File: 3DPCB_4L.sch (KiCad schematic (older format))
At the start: 194 parts, among them IC1 DRV8825, IC2 DRV8825, IC3 DRV8825, IC4 DRV8825, IC5 DRV8825, J1 SOLDER_JUMPER_3P, J10 , J11 , J12 , J13 , J14 , J15 , J16 , J2 , J3 , J4 , J5 , J6 , J7 , J8 , J9 , K1 CONN_3, K2 CONN_3, K3 CONN_3, K4 CONN_3, K5 CONN_3, K6 CONN_3, K7 CONN_3, K8 CONN_3, K9 CONN_3, P1 CONN_8, P10 CONN_2, P11 CONN_3X2, P12 CONN_3X2, P13 CONN_4, P2 CONN_2, P3 CONN_2, P4 CONN_2, P5 CONN_4, P6 CONN_4, P7 CONN_4, P8 CONN_2, P9 CONN_4, U1 CONN_4_LERCHE, U10 MICRO-SD, U11 TC4427, U12 MCP4728, U13 CONN_4_LERCHE, U15 SPST_MOMENTARY, U16 CONN_4_LERCHE, U17 TC4427, U2 SPST_MOMENTARY, U20 TPS6213X, U21 CONN_4_LERCHE, U22 CONN_4_LERCHE, U23 MCP4728, U24 MOS_NFET, U25 CONN_4_LERCHE, U3 BSS84, U4 CONN_4_LERCHE, U5 MOS_NFET, U6 LPC1768_TQFP100, U7 MOS_NFET, U8 MOS_NFET

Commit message: Trying MP9943 DC to DC
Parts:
- removed C47: 3.3nF, ~, symbol C
- removed U20: TPS6213X, symbol TPS6213X
- added C?: 100uF, ~, symbol CP
- added C?: 100n, ~, symbol C
- added IC?: MP9943, ~, symbol MP9943
- added R?: 1M, ~, symbol R
- added R?: 20R, ~, symbol R
- added R?: 51k, ~, symbol R
- added R?: 41k2, ~, symbol R
- added R?: 13k, ~, symbol R
- C43: value 100uF -> 47uF
- L2: value INDUCTOR -> 10uH
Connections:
- wire segments 394 -> 401
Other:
- moved on the sheet: C2, C44, C45, C46, C6, D9, L2

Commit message: Needs to make MP9943 footprint for PCB
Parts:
- gave numbers to parts that had none: 9

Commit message: PCB routed, needs specific BOM
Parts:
- removed C48, C49, C56, C57, C58, C59, C60, C61: 100n, ~, symbol C
- removed C55: 10uF, ~, symbol CP
- removed D10: DIODE, ~, symbol DIODE
- removed J1: SOLDER_JUMPER_3P, ~, symbol SOLDER_JUMPER_3P
- removed P10, P2, P3, P4: CONN_2, symbol CONN_2
- removed R17, R25, R26, R49, R50, R51: 1k, ~, symbol R
- removed R46, R47, R48, R52, R53, R54: 5k6, ~, symbol R
- removed VREG1: AMS1117, ~, symbol AMS1117
- added P2: CONN_8, symbol CONN_8
- added R56, R57, R58, R59: 3k, ~, symbol R
- L2: value 10uH -> IHLP1212-10uH
- R14, R15, R16, R20: value 4K7 -> 9k
- U11, U17: value TC4427 -> IX4427
- U24, U5, U7, U8: value MOS_NFET -> IRFH7932
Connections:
- net labels added: P2.4, P2.5, VDCVDC
- net labels removed: +5V, PWM0, PWM1, X-MAX-LPC, X-MIN-LPC, Y-MAX-LPC, Y-MIN-LPC, Z-MAX-LPC, Z-MIN-LPC
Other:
- note removed: "MOSFET: IRFH7932"
- note removed: "MOSFETS: STL60N3LLH5"
- moved on the sheet: K1, K2, K3, K4, K5, K6, R14, R15, R16, R20, U11A, U11B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

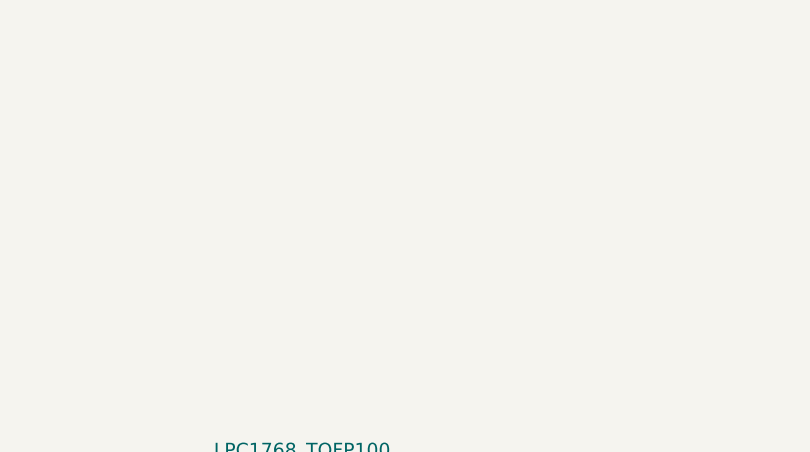
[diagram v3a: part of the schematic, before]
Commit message: All PCB is routed - PCB sent to production
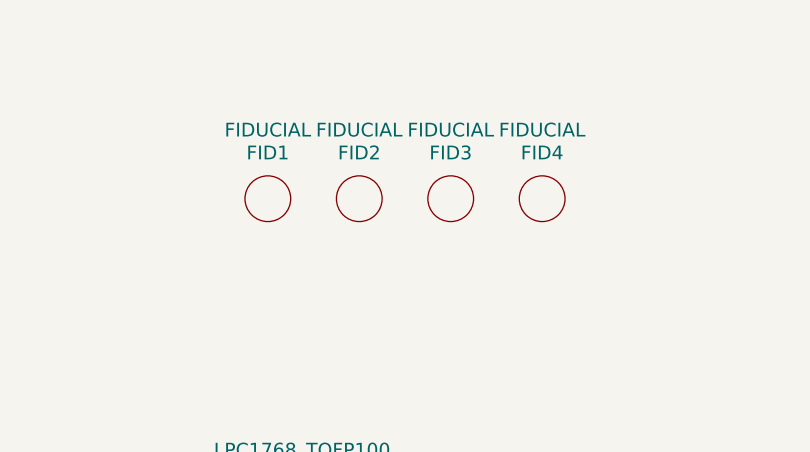
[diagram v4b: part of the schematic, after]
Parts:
- added FID1, FID2, FID3, FID4: FIDUCIAL, symbol FIDUCIAL
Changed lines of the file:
@@
 Sheet 1 1
 Title "3DPCB"
-Date "24 aug 2015"
+Date "14 sep 2015"
 Rev "C"
 Comp "LercheTech"
@@
 Connection ~ 13400 13150
 Connection ~ 13400 12950
+$Comp
+L FIDUCIAL FID1
+U 1 1 55F69685
+P 7100 1050
+F 0 "FID1" H 7100 1250 60  0000 C CNN
+F 1 "FIDUCIAL" H 7100 1350 60  0000 C CNN
+F 2 "" H 7100 1050 60  0000 C CNN
+F 3 "" H 7100 1050 60  0000 C CNN
+	1    7100 1050
+	1    0    0    -1
+$EndComp
+$Comp
+L FIDUCIAL FID2
+U 1 1 55F69692
+P 7500 1050
+F 0 "FID2" H 7500 1250 60  0000 C CNN
+F 1 "FIDUCIAL" H 7500 1350 60  0000 C CNN
+F 2 "" H 7500 1050 60  0000 C CNN
+F 3 "" H 7500 1050 60  0000 C CNN
+	1    7500 1050
+	1    0    0    -1
+$EndComp
+$Comp
+L FIDUCIAL FID3
+U 1 1 55F69698
+P 7900 1050
+F 0 "FID3" H 7900 1250 60  0000 C CNN
+F 1 "FIDUCIAL" H 7900 1350 60  0000 C CNN
+F 2 "" H 7900 1050 60  0000 C CNN
+F 3 "" H 7900 1050 60  0000 C CNN
+	1    7900 1050
+	1    0    0    -1
+$EndComp
+$Comp
+L FIDUCIAL FID4
+U 1 1 55F6969E
+P 8300 1050
+F 0 "FID4" H 8300 1250 60  0000 C CNN
+F 1 "FIDUCIAL" H 8300 1350 60  0000 C CNN
+F 2 "" H 8300 1050 60  0000 C CNN
+F 3 "" H 8300 1050 60  0000 C CNN
+	1    8300 1050
+	1    0    0    -1
+$EndComp
 $EndSCHEMATC

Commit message: Removed soldermask from stackup-info
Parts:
- U24, U5, U7, U8: value IRFH7932 -> IRFH5302
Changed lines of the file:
@@
 Sheet 1 1
 Title "3DPCB"
-Date "14 sep 2015"
+Date "15 sep 2015"
 Rev "C"
 Comp "LercheTech"
@@
 P 9250 13250
 F 0 "U5" H 9650 13200 60  0000 C CNN
-F 1 "IRFH7932" H 9650 13300 60  0000 C CNN
+F 1 "IRFH5302" H 9650 13300 60  0000 C CNN
 F 2 "~" H 9350 13250 60  0000 C CNN
 F 3 "~" H 9350 13250 60  0000 C CNN
@@
 P 11900 13250
 F 0 "U7" H 12300 13200 60  0000 C CNN
-F 1 "IRFH7932" H 12300 13300 60  0000 C CNN
+F 1 "IRFH5302" H 12300 13300 60  0000 C CNN
 F 2 "~" H 12000 13250 60  0000 C CNN
 F 3 "~" H 12000 13250 60  0000 C CNN
@@
 P 9250 14500
 F 0 "U8" H 9650 14450 60  0000 C CNN
-F 1 "IRFH7932" H 9650 14550 60  0000 C CNN
+F 1 "IRFH5302" H 9650 14550 60  0000 C CNN
 F 2 "~" H 9350 14500 60  0000 C CNN
 F 3 "~" H 9350 14500 60  0000 C CNN
@@
 P 11900 14500
 F 0 "U24" H 12300 14450 60  0000 C CNN
-F 1 "IRFH7932" H 12300 14550 60  0000 C CNN
+F 1 "IRFH5302" H 12300 14550 60  0000 C CNN
 F 2 "~" H 12000 14500 60  0000 C CNN
 F 3 "~" H 12000 14500 60  0000 C CNN

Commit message: Added LercheTech library
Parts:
- C1, C12, C13, C14, C15, C16, C17, C18, C19, C2, C20, C22, C23, C28, C29, C30, C31, C32, C33, C34, C35, C36, C37, C38, C39, C40, C41, C42, C44, C45, C46, C5, C50, C51, C52, C53, C54, C6, C64, C65, C67, C68, C69, C71, C8, C9: symbol C -> C-RESCUE-3DPCB_4L
- C10, C11, C24, C25, C26, C27, C3, C4, C43, C7, C70: symbol CP -> CP-RESCUE-3DPCB_4L
- D1, D2, D3, D4, D6, D7, D8: symbol LED -> LED-RESCUE-3DPCB_4L
- R1, R10, R11, R12, R13, R14, R15, R16, R18, R19, R2, R20, R21, R22, R23, R24, R27, R28, R29, R3, R30, R31, R32, R33, R34, R35, R36, R37, R38, R39, R4, R40, R41, R42, R43, R44, R45, R5, R55, R56, R57, R58, R59, R6, R7, R8, R9: symbol R -> R-RESCUE-3DPCB_4L

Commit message: Updated
local repository + minor change to allow 24V on MOSFET drivers.
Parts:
- removed U17: IX4427, symbol TC4427
- added C21, C47: 100n, LercheTech:Lerche_C0603, symbol C-RESCUE-3DPCB_4L
- added C49: 1uF, LercheTech:Lerche_C0603, symbol C
- added D10: Vz10V/0.5W, Diodes_SMD:SMA_Standard, symbol ZENERsmall
- added R17: 1k, Resistors_SMD:R_0805, symbol R
- added U9: TC4427, SMD_Packages:SOIC-8-N, symbol TC4427
- C1, C12, C13, C14, C15, C16, C17, C18, C19, C2, C20, C22, C23, C28, C29, C30, C31, C32, C33, C34, C35, C36, C37, C38, C39, C40, C41, C42, C44, C45, C46, C5, C50, C51, C52, C53, C54, C6, C64, C65, C67, C68, C69, C71, C8, C9: footprint ~ -> LercheTech:Lerche_C0603
- C10, C3, C4, C7: footprint ~ -> Capacitors_Tantalum_SMD:TantalC_SizeA_EIA-3216_Reflow
- C11, C24, C25, C26, C27, C70: footprint ~ -> Capacitors_ThroughHole:C_Radial_D6.3_L11.2_P2.5
- C43: footprint ~ -> Capacitors_SMD:c_elec_5x5.8
- CONN1: footprint ~ -> LercheTech:Lerche_MINI_USB
- D1, D2, D3, D4, D6, D7, D8: footprint ~ -> LEDs:LED_0603
- D5, D9: footprint ~ -> LercheTech:Lerche_SOD323
- FID1, FID2, FID3, FID4: footprint (none) -> LercheTech:Lerche_Fiducial
- IC1, IC2, IC3, IC4, IC5: footprint ~ -> LercheTech:Lerche_TSSOP28_EP
- IC6: footprint ~ -> LercheTech:Lerche_MP9943
- J10, J11, J12, J13, J14, J15, J16, J2, J3, J4, J5, J6, J7, J8, J9: footprint ~ -> LercheTech:Lerche_2PsolderJumper
- K1, K2, K3, K4, K5, K6, K8, K9: footprint (none) -> Pin_Headers:Pin_Header_Straight_1x03
- K7: footprint (none) -> LercheTech:Lerche_3P_1.27MM
- L1, R1, R10, R11, R12, R13, R18, R19, R2, R27, R28, R3, R34, R35, R36, R38, R39, R4, R40, R41, R42, R43, R44, R45, R5, R55, R6, R7, R8, R9: footprint ~ -> LercheTech:Lerche_R0603
- L2: footprint ~ -> LercheTech:Lerche_IHLP-1212BZ-11_Inductor
- OSC1: footprint (none) -> LercheTech:Lerche_Oscillator_2.5x2.0mm
- P1: footprint (none) -> LercheTech:Lerche_8P_2.54mm
- P11: footprint (none) -> Pin_Headers:Pin_Header_Straight_2x03
- P12: footprint (none) -> LercheTech:Lerche_6P_1.6mm_2ROW
- P13, P5, P6, P7, P9: footprint (none) -> LercheTech:Lerche_4P_2.54mm
- P2: footprint (none) -> LercheTech:Lerche_8P_CONN_3,5mm
- P8: footprint (none) -> LercheTech:Lerche_2P_5MM
- R14, R15, R16, R20: value 9k -> 47k; footprint ~ -> LercheTech:Lerche_R0603
- R21, R22, R23, R24, R29, R30, R31, R32, R33, R37: footprint ~ -> LercheTech:Lerche_R1206
- R56, R57, R58, R59: value 3k -> 10R; footprint ~ -> LercheTech:Lerche_R0603
- U1, U13, U16, U21, U22, U25, U4: footprint ~ -> LercheTech:Lerche_4P_2.54mm
- U10: footprint (none) -> LercheTech:Lerche_Molex_502774-0891
- U11: value IX4427 -> TC4427; footprint (none) -> SMD_Packages:SOIC-8-N
- U12, U23: footprint (none) -> LercheTech:Lerche_MSOP-10
- U15, U2: footprint ~ -> LercheTech:Lerche_SPST_ITEAD
- U24, U5, U7, U8: footprint ~ -> LercheTech:Lerche_PQFN_5x6B
- U3: footprint ~ -> LercheTech:Lerche_SOT23-3
- U6: footprint ~ -> Housings_QFP:TQFP-100_14x14mm_Pitch0.5mm
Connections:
- net +12V: now also R17.1; no longer U11.6 (Vdd), U11.6 (Vdd)
- net GND: now also C21.2, C47.2, C49.2, D10.2 (A), U9.3 (GND); no longer U11.3 (GND)
- net P2.4: now also U9.2 (IN)
- net P2.5: now also U9.4 (IN)
- net at R56.1: now also U9.7 (OUT)
- net at R58.1: now also U9.5 (OUT)
- new net MOSVCC: C21.1, C47.1, C49.1, D10.1 (K), R17.2, U11.6 (Vdd), U9.6 (Vdd)
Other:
- note added: "+24V connector"
- note added: "Caps for stepper drivers"
- note added: "DAC's for stepper current control"
- note added: "DC/DC Converter"
- note added: "Endstop inputs"
- note added: "I2C connection"
- note added: "LED's"
- note added: "MOSFET outputs"
- note added: "Micro-SD"
- note added: "Pinheader output for stepper drivers"
- note added: "Provided as-is.\nThis is 3DPCB, a board for driving 3D printers, CNC's and what else is possible using the onboard equipment. \nThe design is based around Smoothieware, and Smoothieboard, but some things are done differently. \nThe onboard DC/DC converter makes it possible to connect up to maximum 27V, and drive the steppers with this voltage. \n"
- note added: "Reset and Play button"
- note added: "SPI pinout"
- note added: "SPI_SD pinout"
- note added: "Stepper drivers"
- note added: "Thermistor inputs"
- note added: "Todo: Switch to IRFH7085TRPBF MOSFET transistors"
- note added: "UART0 pinout"
- note added: "USB connector"
- moved on the sheet: C22, C23, C24, C25, C26, C27, C28, C29, C30, C31, C32, C33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

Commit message: Updated PCB
Updated PCB, splitting power for MOSFETs and motor-drivers.
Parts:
- removed P8: CONN_2, LercheTech:Lerche_2P_5MM, symbol CONN_2
- added P8: CONN_02X03, symbol CONN_02X03
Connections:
- net +12V: now also P8.2 (P2); no longer P2.2 (P2), P2.4 (P4), P2.6 (P6), P2.8 (P8), R17.1
- net GND: now also P8.1 (P1), P8.4 (P4), P8.6 (P6)
- new net V_MOSFET: P2.2 (P2), P2.4 (P4), P2.6 (P6), P2.8 (P8), P8.3 (P3), P8.5 (P5), R17.1
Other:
- note added: "Molex UltraFit power connector"
- note added: "Todo: Switch to IRFH7085TRPBF MOSFETs"
- note removed: "+24V connector"
- note removed: "Todo: Switch to IRFH7085TRPBF MOSFET transistors"
- moved on the sheet: K7, P11
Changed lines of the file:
@@
 LIBS:contrib
 LIBS:valves
-LIBS:lerchetech (1)
+LIBS:lerchetech
 LIBS:3DPCB_4L-cache
 EELAYER 25 0
@@
 P2.6
 $Comp
-L +12V #PWR87
-U 1 1 524C0A34
-P 15450 10600
-F 0 "#PWR87" H 15450 10550 20  0001 C CNN
-F 1 "+12V" H 15450 10700 30  0000 C CNN
-F 2 "" H 15450 10600 60  0000 C CNN
-F 3 "" H 15450 10600 60  0000 C CNN
-	1    15450 10600
-	1    0    0    -1
-$EndComp
-$Comp
 L C-RESCUE-3DPCB_4L C16
 U 1 1 524C17C4
@@
 L GND-RESCUE-3DPCB_4L #PWR7
 U 1 1 524B7E4F
-P 1350 4400
-F 0 "#PWR7" H 1350 4400 30  0001 C CNN
-F 1 "GND" H 1350 4330 30  0001 C CNN
-F 2 "" H 1350 4400 60  0000 C CNN
-F 3 "" H 1350 4400 60  0000 C CNN
-	1    1350 4400
+P 1750 4500
+F 0 "#PWR7" H 1750 4500 30  0001 C CNN
+F 1 "GND" H 1750 4430 30  0001 C CNN
+F 2 "" H 1750 4500 60  0000 C CNN
+F 3 "" H 1750 4500 60  0000 C CNN
+	1    1750 4500
 	1    0    0    -1
 $EndComp
@@
 L +12V #PWR6
 U 1 1 524B816D
-P 1350 3950
-F 0 "#PWR6" H 1350 3900 20  0001 C CNN
-F 1 "+12V" H 1350 4050 30  0000 C CNN
-F 2 "" H 1350 3950 60  0000 C CNN
-F 3 "" H 1350 3950 60  0000 C CNN
-	1    1350 3950
+P 1750 4100
+F 0 "#PWR6" H 1750 4050 20  0001 C CNN
+F 1 "+12V" H 1750 4200 30  0000 C CNN
+F 2 "" H 1750 4100 60  0000 C CNN
+F 3 "" H 1750 4100 60  0000 C CNN
+	1    1750 4100
 	1    0    0    -1
 $EndComp
@@
 L CONN_3 K7
 U 1 1 5253846A
-P 1650 4150
-F 0 "K7" V 1600 4150 50  0000 C CNN
-F 1 "CONN_3" V 1700 4150 40  0000 C CNN
-F 2 "LercheTech:Lerche_3P_1.27MM" H 1650 4150 60  0001 C CNN
-F 3 "" H 1650 4150 60  0000 C CNN
-	1    1650 4150
+P 2350 4150
+F 0 "K7" V 2300 4150 50  0000 C CNN
+F 1 "CONN_3" V 2400 4150 40  0000 C CNN
+F 2 "LercheTech:Lerche_3P_1.27MM" H 2350 4150 60  0001 C CNN
+F 3 "" H 2350 4150 60  0000 C CNN
+	1    2350 4150
 	-1   0    0    -1
 $EndComp
-Text GLabel 2000 4050 2    39   Input ~ 0
+Text GLabel 2700 4050 2    39   Input ~ 0
 TX_0
-Text GLabel 2000 4150 2    39   Input ~ 0
+Text GLabel 2700 4150 2    39   Input ~ 0
 RX_0
-Text GLabel 2000 4250 2    39   Input ~ 0
+Text GLabel 2700 4250 2    39   Input ~ 0
 GND
 Text Label 11550 10850 2    39   ~ 0
@@
 PLAY_LED
 $Comp
-L CONN_2 P8
-U 1 1 5258344A
-P 1000 4150
-F 0 "P8" V 950 4150 40  0000 C CNN
-F 1 "CONN_2" V 1050 4150 40  0000 C CNN
-F 2 "LercheTech:Lerche_2P_5MM" H 1000 4150 60  0001 C CNN
-F 3 "" H 1000 4150 60  0000 C CNN
-	1    1000 4150
-	-1   0    0    1
-$EndComp
-$Comp
 L +3.3V-RESCUE-3DPCB_4L #PWR3
 U 1 1 52584578
@@
 L GND-RESCUE-3DPCB_4L #PWR33
 U 1 1 525FF499
-P 2500 4350
-F 0 "#PWR33" H 2500 4350 30  0001 C CNN
-F 1 "GND" H 2500 4280 30  0001 C CNN
-F 2 "" H 2500 4350 60  0000 C CNN
-F 3 "" H 2500 4350 60  0000 C CNN
-	1    2500 4350
+P 3200 4350
+F 0 "#PWR33" H 3200 4350 30  0001 C CNN
+F 1 "GND" H 3200 4280 30  0001 C CNN
+F 2 "" H 3200 4350 60  0000 C CNN
+F 3 "" H 3200 4350 60  0000 C CNN
+	1    3200 4350
 	-1   0    0    -1
 $EndComp
-Text GLabel 3400 4050 2    39   Input ~ 0
+Text GLabel 4100 4050 2    39   Input ~ 0
 SSEL1
-Text GLabel 2600 4050 0    39   Input ~ 0
+Text GLabel 3300 4050 0    39   Input ~ 0
 MISO1
-Text GLabel 2600 4150 0    39   Input ~ 0
+Text GLabel 3300 4150 0    39   Input ~ 0
 MOSI1
-Text GLabel 3400 4150 2    39   Input ~ 0
+Text GLabel 4100 4150 2    39   Input ~ 0
 SCK1
 $Comp
@@
 L CONN_3X2 P11
 U 1 1 5368F485
-P 3000 4200
-F 0 "P11" H 3000 4450 50  0000 C CNN
-F 1 "CONN_3X2" V 3000 4250 40  0000 C CNN
-F 2 "Pin_Headers:Pin_Header_Straight_2x03" H 3000 4200 60  0001 C CNN
-F 3 "" H 3000 4200 60  0000 C CNN
-	1    3000 4200
+P 3700 4200
+F 0 "P11" H 3700 4450 50  0000 C CNN
+F 1 "CONN_3X2" V 3700 4250 40  0000 C CNN
+F 2 "Pin_Headers:Pin_Header_Straight_2x03" H 3700 4200 60  0001 C CNN
+F 3 "" H 3700 4200 60  0000 C CNN
+	1    3700 4200
 	1    0    0    -1
 $EndComp
@@
 L +3.3V-RESCUE-3DPCB_4L #PWR40
 U 1 1 5368F764
-P 3500 4350
-F 0 "#PWR40" H 3500 4310 30  0001 C CNN
-F 1 "+3.3V" H 3500 4460 30  0000 C CNN
-F 2 "" H 3500 4350 60  0000 C CNN
-F 3 "" H 3500 4350 60  0000 C CNN
-	1    3500 4350
+P 4200 4350
+F 0 "#PWR40" H 4200 4310 30  0001 C CNN
+F 1 "+3.3V" H 4200 4460 30  0000 C CNN
+F 2 "" H 4200 4350 60  0000 C CNN
+F 3 "" H 4200 4350 60  0000 C CNN
+	1    4200 4350
 	-1   0    0    1
 $EndComp
@@
 	2400 9100 2400 9200
 Wire Wire Line
-	1350 3950 1350 4050
-Wire Wire Line
-	1350 4250 1350 4400
-Wire Wire Line
 	6500 11600 6900 11600
 Connection ~ 6700 11600
@@
 	1450 3500 1450 3550
 Wire Wire Line
-	2600 4250 2500 4250
+	3300 4250 3200 4250
 Wire Wire Line
-	2500 4250 2500 4350
+	3200 4250 3200 4350
 Wire Wire Line
-	3400 4250 3500 4250
+	4100 4250 4200 4250
 Wire Wire Line
-	3500 4250 3500 4350
+	4200 4250 4200 4350
 Wire Wire Line
 	1550 11250 1550 12050
@@
 Text Notes 2950 3600 0    60   ~ 0
 SPI_SD pinout
-Text Notes 2750 4450 0    60   ~ 0
+Text Notes 3450 4450 0    60   ~ 0
 SPI pinout
-Text Notes 1550 4400 0    60   ~ 0
+Text Notes 2250 4400 0    60   ~ 0
 UART0 pinout
-Text Notes 550  3950 0    60   ~ 0
-+24V connector
+Text Notes 700  3950 0    60   ~ 0
+Molex UltraFit power connector
 Text Notes 1550 700  0    60   ~ 0
 DC/DC Converter
@@
 	9450 10050 9450 10150
 Text Notes 13500 13350 0    60   ~ 0
-Todo: Switch to IRFH7085TRPBF MOSFET transistors
+Todo: Switch to IRFH7085TRPBF MOSFETs
 $Comp
 L TC4427 U9
@@
 	7800 12950 7800 13100
 Connection ~ 7950 12950
-$Comp
-L +12V #PWR52
-U 1 1 5811C3C8
-P 7950 12300
-F 0 "#PWR52" H 7950 12250 20  0001 C CNN
-F 1 "+12V" H 7950 12400 30  0000 C CNN
-F 2 "" H 7950 12300 60  0000 C CNN
-F 3 "" H 7950 12300 60  0000 C CNN
-	1    7950 12300
-	1    0    0    -1
-$EndComp
-Wire Wire Line
-	7950 12300 7950 12400
 Wire Wire Line
 	9300 12950 9300 13150
@@
 Text GLabel 9450 9650 0    39   Input ~ 0
 MOSVCC
+$Comp
+L CONN_02X03 P8
+U 1 1 582DF4EB
+P 1400 4300
+F 0 "P8" H 1400 4500 50  0000 C CNN
+F 1 "CONN_02X03" H 1400 4100 50  0000 C CNN
+F 2 "" H 1400 3100 50  0000 C CNN
+F 3 "" H 1400 3100 50  0000 C CNN
+	1    1400 4300
+	1    0    0    -1
+$EndComp
+Text GLabel 15450 10600 1    60   Input ~ 0
+V_MOSFET
+Text GLabel 1150 4300 0    39   Input ~ 0
+V_MOSFET
+Text GLabel 1150 4400 0    39   Input ~ 0
+V_MOSFET
+Wire Wire Line
+	1650 4400 1750 4400
+Wire Wire Line
+	1750 4300 1750 4500
+Wire Wire Line
+	1650 4300 1750 4300
+Connection ~ 1750 4400
+Wire Wire Line
+	1650 4200 1750 4200
+Wire Wire Line
+	1750 4200 1750 4100
+$Comp
+L GND-RESCUE-3DPCB_4L #PWR?
+U 1 1 582FAF15
+P 700 4500
+F 0 "#PWR?" H 700 4500 30  0001 C CNN
+F 1 "GND" H 700 4430 30  0001 C CNN
+F 2 "" H 700 4500 60  0000 C CNN
+F 3 "" H 700 4500 60  0000 C CNN
+	1    700  4500
+	1    0    0    -1
+$EndComp
+Wire Wire Line
+	1150 4200 700  4200
+Wire Wire Line
+	700  4200 700  4500
+Text GLabel 7950 12400 1    60   Input ~ 0
+V_MOSFET
 $EndSCHEMATC
